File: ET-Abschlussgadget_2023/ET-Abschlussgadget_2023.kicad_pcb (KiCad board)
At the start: 2 copper layers, 85 x 54 mm, 23 parts, among them U1 ATtiny10-TS

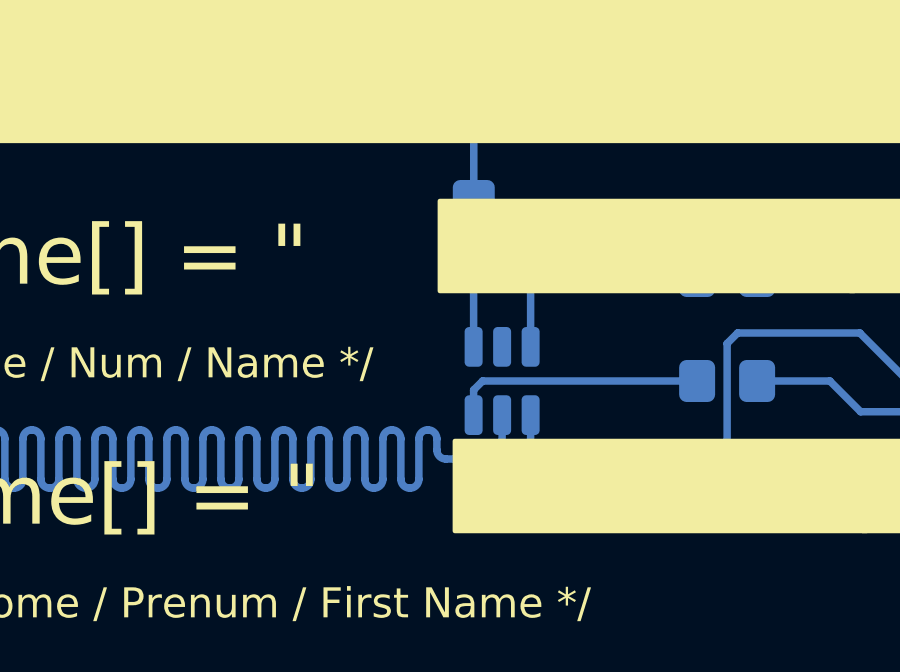
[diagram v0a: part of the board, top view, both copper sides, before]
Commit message: Add bypass capacitor
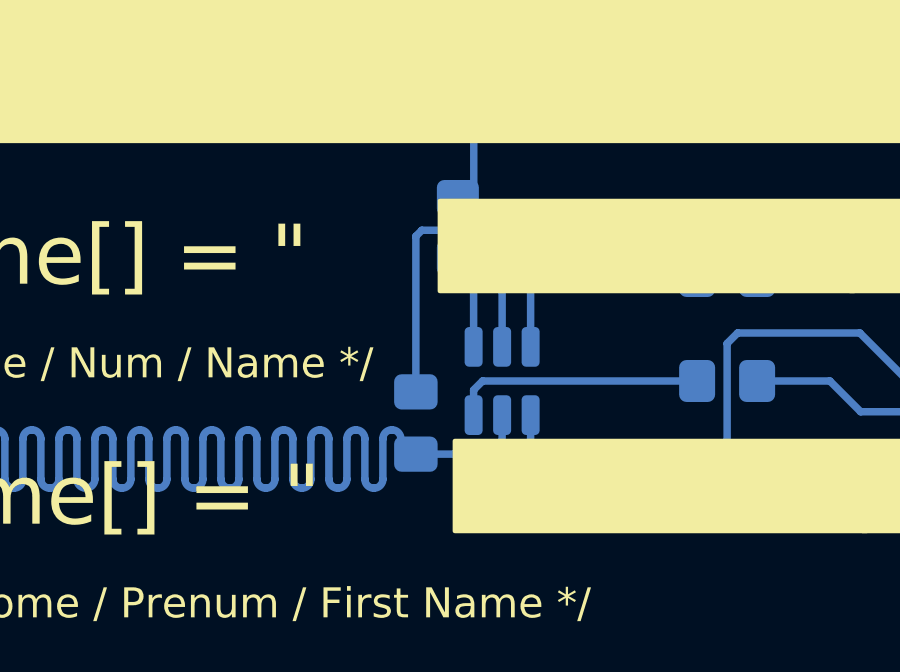
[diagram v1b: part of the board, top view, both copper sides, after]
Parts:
- added C1: 100nF, Capacitor_SMD:C_0805_2012Metric_Pad1.18x1.45mm_HandSolder, B.Cu at (135.0, 108.4)
- moved R4 0.53 mm to (136.4, 101.9)
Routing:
- net GND: track 0.00 -> 11.9 mm
- net VCC: track 116.3 -> 111.7 mm

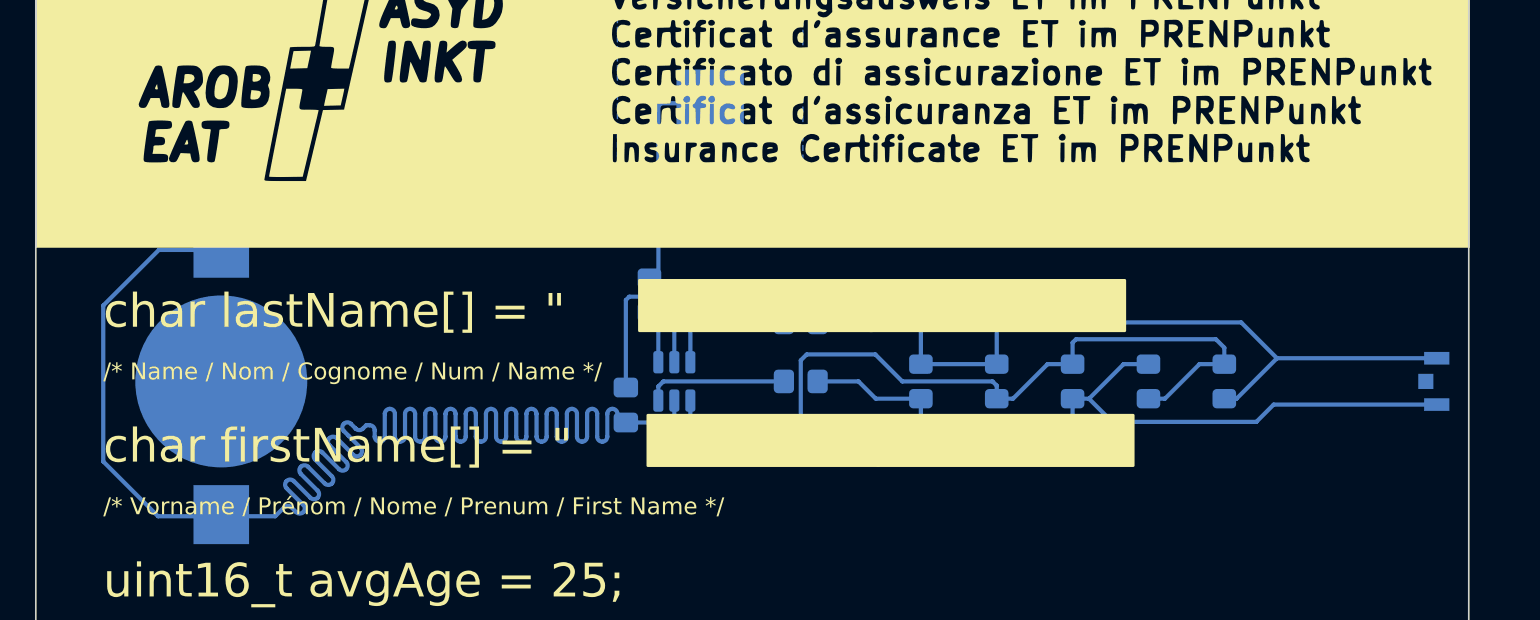
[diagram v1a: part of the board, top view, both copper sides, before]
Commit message: Add rounded tracks
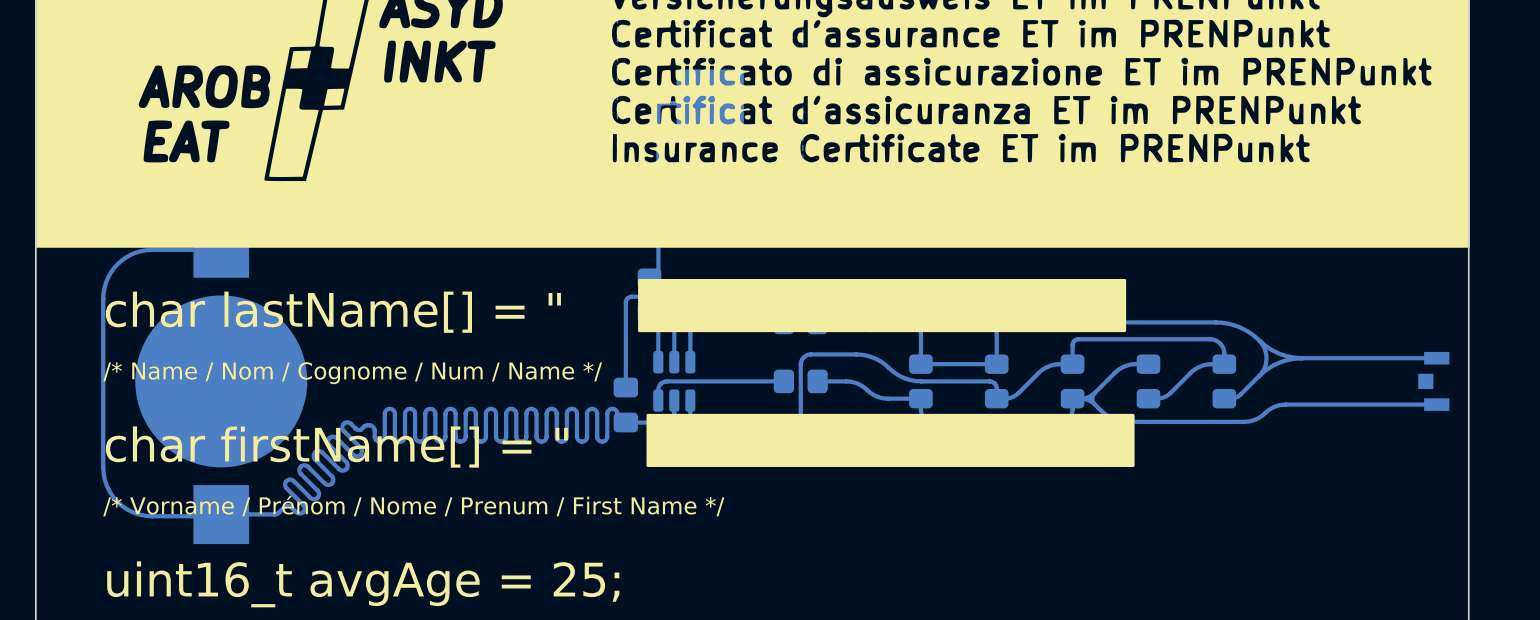
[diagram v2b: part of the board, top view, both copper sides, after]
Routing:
- net Net-(D1-K): track 46.5 -> 49.6 mm
- net VCC: track 111.7 -> 112.8 mm
- net Net-(D1-A): track 41.2 -> 40.2 mm

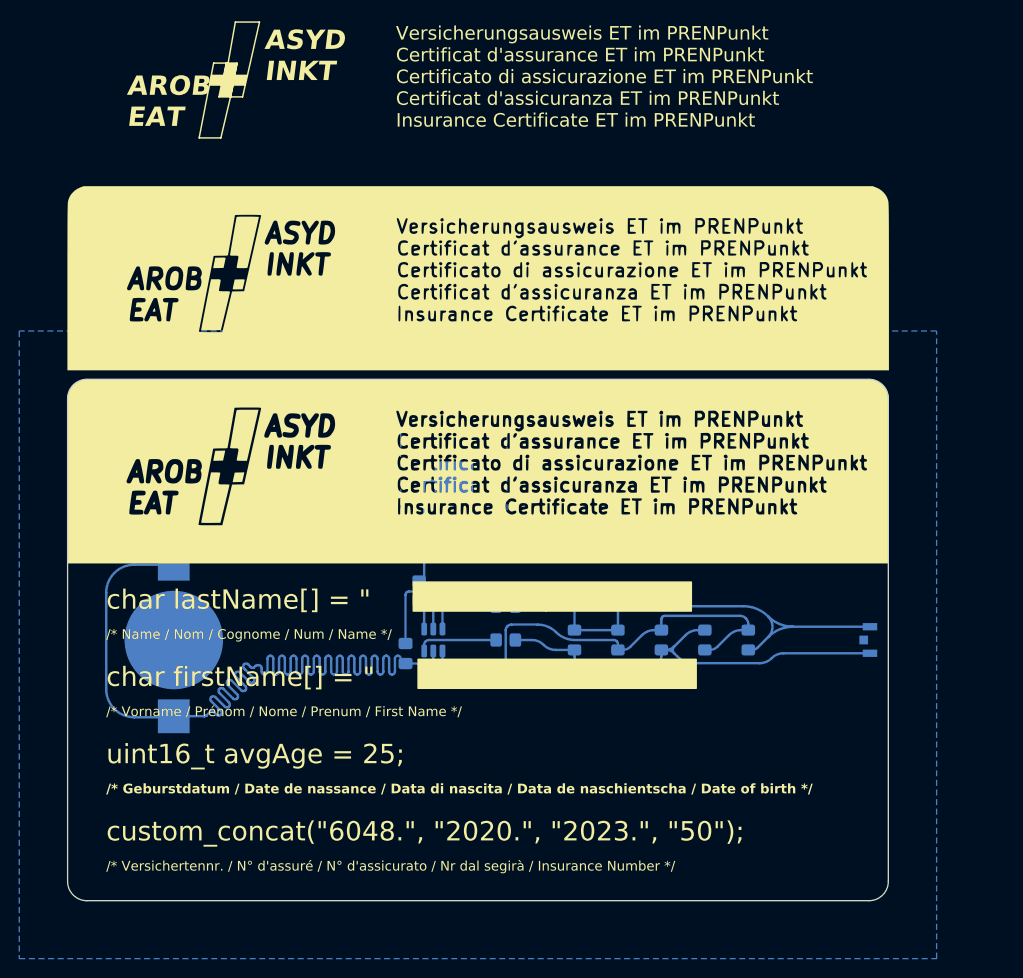
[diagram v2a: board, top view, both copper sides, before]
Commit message: Add copper to front, Improve sillkscreen
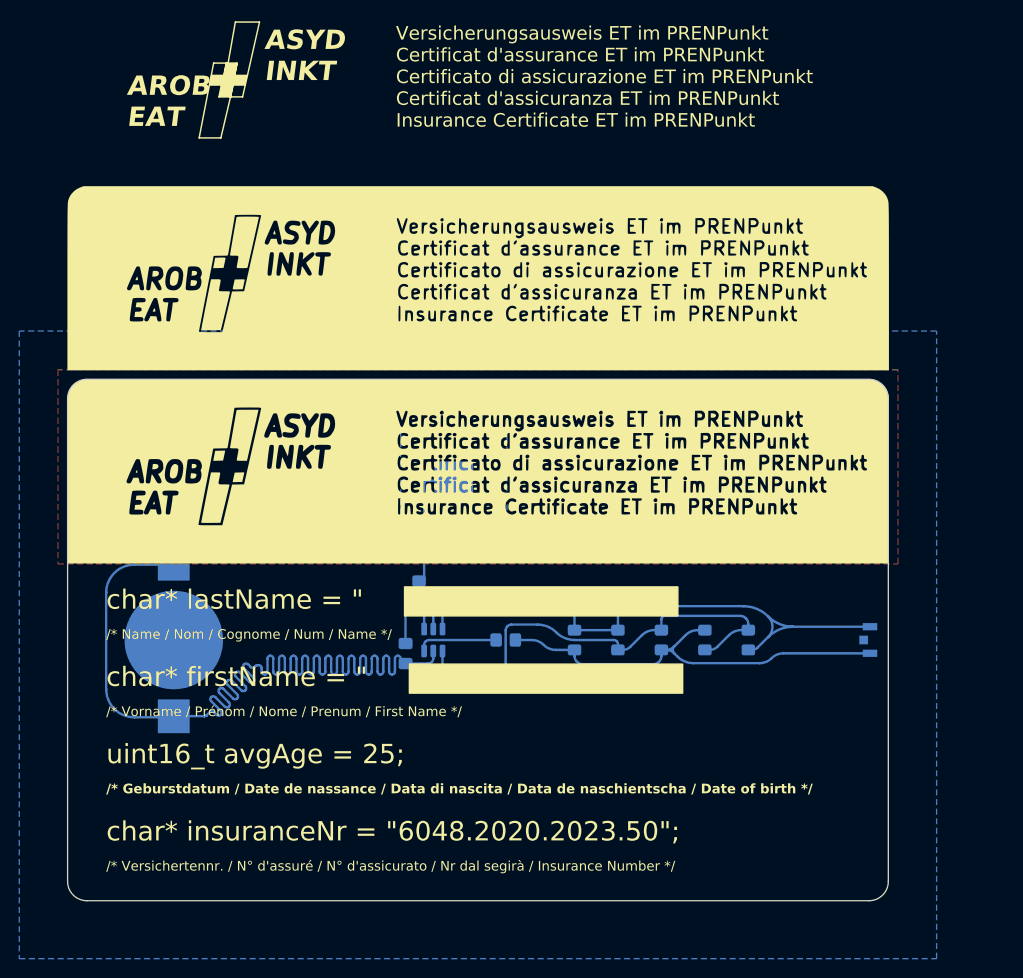
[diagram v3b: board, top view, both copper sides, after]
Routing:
- added copper zone on F.Cu, net (none)
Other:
- board text added: "char* firstName = {dblquote} {dblquote};"
- board text added: "char* insuranceNr = {dblquote}6048.2020.2023.50{dblquote};"
- board text added: "char* lastName = {dblquote} {dblquote};"
- board text removed: "char firstName[] = {dblquote} {dblquote};"
- board text removed: "char lastName[] = {dblquote} {dblquote};"
- board text removed: "custom_concat({dblquote}6048.{dblquote}, {dblquote}2020.{dblquote}, {dblquote}2023.{dblquote}, {dblquote}50{dblquote});"
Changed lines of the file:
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@@
     (attr board_only exclude_from_pos_files exclude_from_bom)
     (fp_text reference "kibuzzard-642F12E3" (at 0 4.715933 90) (layer "B.SilkS") hide
-        (effects (font (size 0 0)) (justify mirror))
+        (effects (font (size 0 0) (thickness 0.15)) (justify mirror))
     )
     (fp_text value "G***" (at 0 -4.715933 90) (layer "B.SilkS") hide
-        (effects (font (size 0 0)) (justify mirror))
+        (effects (font (size 0 0) (thickness 0.15)) (justify mirror))
     )
     (fp_poly
@@
     (attr board_only exclude_from_pos_files exclude_from_bom)
     (fp_text reference "kibuzzard-642F12C7" (at 0 4.692121 90) (layer "B.SilkS") hide
-        (effects (font (size 0 0)) (justify mirror))
+        (effects (font (size 0 0) (thickness 0.15)) (justify mirror))
     )
     (fp_text value "G***" (at 0 -4.692121 90) (layer "B.SilkS") hide
-        (effects (font (size 0 0)) (justify mirror))
+        (effects (font (size 0 0) (thickness 0.15)) (justify mirror))
     )
     (fp_poly
@@
     (attr board_only exclude_from_pos_files exclude_from_bom)
     (fp_text reference "kibuzzard-642F12D5" (at 0 4.692121 90) (layer "B.SilkS") hide
-        (effects (font (size 0 0)) (justify mirror))
+        (effects (font (size 0 0) (thickness 0.15)) (justify mirror))
     )
     (fp_text value "G***" (at 0 -4.692121 90) (layer "B.SilkS") hide
-        (effects (font (size 0 0)) (justify mirror))
+        (effects (font (size 0 0) (thickness 0.15)) (justify mirror))
     )
     (fp_poly
@@
     (attr board_only exclude_from_pos_files exclude_from_bom)
     (fp_text reference "kibuzzard-642F1300" (at 0 4.734983 90) (layer "B.SilkS") hide
-        (effects (font (size 0 0)) (justify mirror))
+        (effects (font (size 0 0) (thickness 0.15)) (justify mirror))
     )
     (fp_text value "G***" (at 0 -4.734983 90) (layer "B.SilkS") hide
-        (effects (font (size 0 0)) (justify mirror))
+        (effects (font (size 0 0) (thickness 0.15)) (justify mirror))
     )
     (fp_poly
@@
     (attr board_only exclude_from_pos_files exclude_from_bom)
     (fp_text reference "kibuzzard-642F12EF" (at 0 4.692121 90) (layer "B.SilkS") hide
-        (effects (font (size 0 0)) (justify mirror))
+        (effects (font (size 0 0) (thickness 0.15)) (justify mirror))
     )
     (fp_text value "G***" (at 0 -4.692121 90) (layer "B.SilkS") hide
-        (effects (font (size 0 0)) (justify mirror))
+        (effects (font (size 0 0) (thickness 0.15)) (justify mirror))
     )
     (fp_poly
@@
     (attr board_only exclude_from_pos_files exclude_from_bom)
     (fp_text reference "kibuzzard-642F1274" (at 0 5.915872 270) (layer "B.SilkS") hide
-        (effects (font (size 0 0)) (justify mirror))
+        (effects (font (size 0 0) (thickness 0.15)) (justify mirror))
     )
     (fp_text value "G***" (at 0 -5.915872 270) (layer "B.SilkS") hide
-        (effects (font (size 0 0)) (justify mirror))
+        (effects (font (size 0 0) (thickness 0.15)) (justify mirror))
     )
     (fp_poly
@@
   (gr_poly
     (pts
-      (xy 136.3 109)
-      (xy 165.1 109)
-      (xy 165.1 112)
-      (xy 136.3 112)
+      (xy 135.4 109.5)
+      (xy 163.7 109.5)
+      (xy 163.7 112.5)
+      (xy 135.4 112.5)
     )
     (stroke (width 0.15) (type solid)) (fill solid) (layer "F.SilkS"))
   (gr_poly
     (pts
-      (xy 135.8 101)
-      (xy 164.6 101)
-      (xy 164.6 104)
-      (xy 135.8 104)
+      (xy 134.9 101.5)
+      (xy 163.2 101.5)
+      (xy 163.2 104.5)
+      (xy 134.9 104.5)
     )
     (stroke (width 0.15) (type solid)) (fill solid) (layer "F.SilkS"))
@@
     (effects (font (size 2 2) (thickness 0.3)) (justify left bottom))
   )
-  (gr_text "char lastName[] = {dblquote}                   {dblquote};" (at 104 104) (layer "F.SilkS")
+  (gr_text "char* lastName = {dblquote}                   {dblquote};" (at 104 104) (layer "F.SilkS")
     (effects (font (size 2 2) (thickness 0.3)) (justify left bottom))
   )
@@
     (effects (font (size 1 1) (thickness 0.2)) (justify left bottom))
   )
-  (gr_text "custom_concat({dblquote}6048.{dblquote}, {dblquote}2020.{dblquote}, {dblquote}2023.{dblquote}, {dblquote}50{dblquote});" (at 104 128) (layer "F.SilkS")
+  (gr_text "char* insuranceNr = {dblquote}6048.2020.2023.50{dblquote};" (at 104 128) (layer "F.SilkS")
     (effects (font (size 2 2) (thickness 0.3)) (justify left bottom))
   )
@@
     (effects (font (size 1 1) (thickness 0.2) bold) (justify left bottom))
   )
-  (gr_text "char firstName[] = {dblquote}                   {dblquote};" (at 104 112) (layer "F.SilkS")
+  (gr_text "char* firstName = {dblquote}                   {dblquote};" (at 104 112) (layer "F.SilkS")
     (effects (font (size 2 2) (thickness 0.3)) (justify left bottom))
   )
@@
   (segment (start 136.925 103.42) (end 136.925 105.8625) (width 0.25) (layer "B.Cu") (net 10))
   (segment (start 136.405 102.9) (end 136.925 103.42) (width 0.25) (layer "B.Cu") (net 10))
+  (zone (net 0) (net_name "") (layer "F.Cu") (hatch edge 0.5)
+    (priority 1)
+    (connect_pads (clearance 0.5))
+    (min_thickness 0.25) (filled_areas_thickness no)
+    (fill yes (thermal_gap 0.5) (thermal_bridge_width 0.5) (island_removal_mode 1) (island_area_min 10))
+    (polygon
+      (pts
+        (xy 99 79)
+        (xy 99 99.1)
+        (xy 186 99.1)
+        (xy 186 79)
+      )
+    )
+  )
   (zone (net 7) (net_name "GND") (layer "B.Cu") (hatch edge 0.5)
     (connect_pads yes (clearance 0.5))

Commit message: Add qr code to silkscreen
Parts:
- added G***: LOGO, LOGO, B.Cu at (108.9, 125.3)
- moved G*** 9.71 mm to (137.7, 122.4)
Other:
- board text added: "ET: {dblquote}Wie WI, nur besser{dblquote}"
- board text removed: "ET: Wie WI, nur besser"

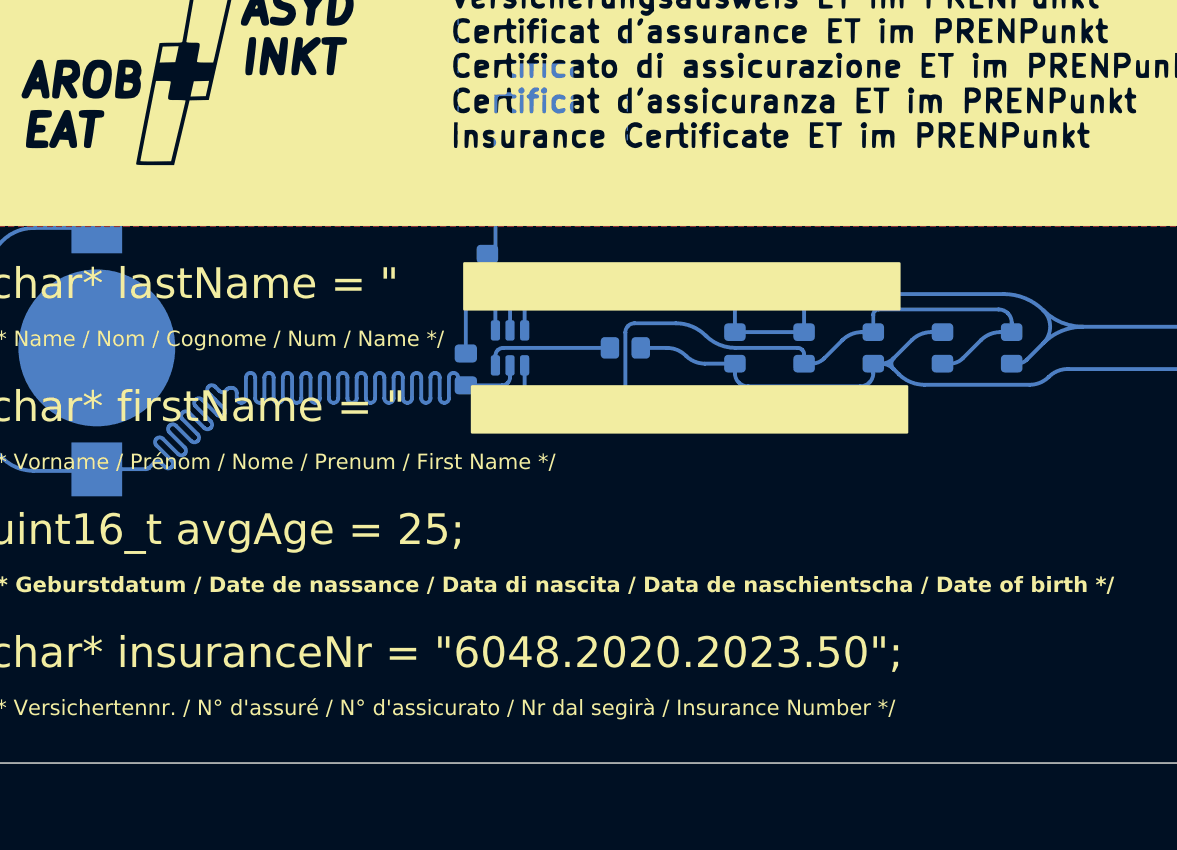
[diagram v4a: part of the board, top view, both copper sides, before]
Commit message: Add switch, Change qr to be smaller
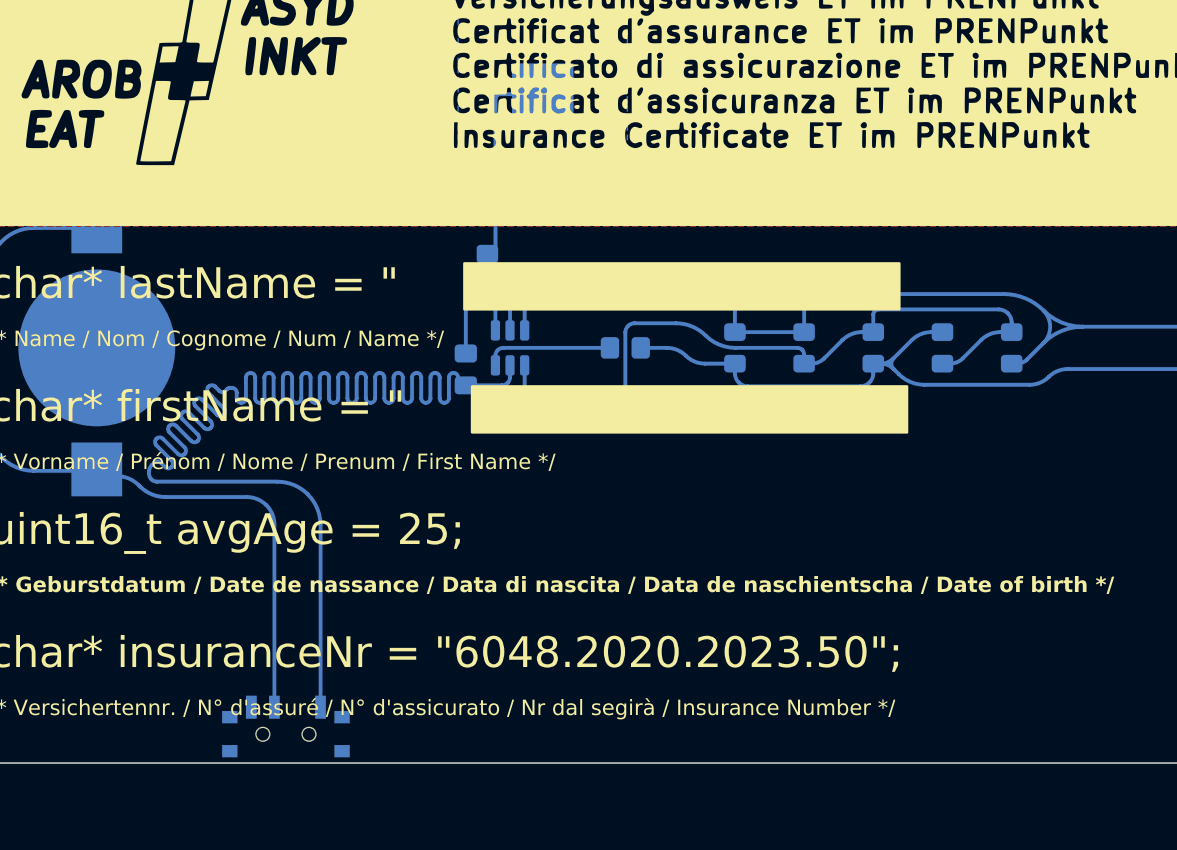
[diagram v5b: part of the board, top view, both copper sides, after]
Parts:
- added SW1: ON/OFF, Button_Switch_SMD:SW_SPDT_PCM12, B.Cu at (123.3, 131.8)
- moved G*** 1.35 mm to (107.9, 126.2)
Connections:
- BT1 pad 1: VCC -> Net-(BT1-+)
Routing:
- net Net-(BT1-+): track 0.00 -> 51.5 mm
- net VCC: track 112.8 -> 107.4 mm
